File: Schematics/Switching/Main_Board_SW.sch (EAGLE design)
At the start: 88 parts, among them IC1 LM317MBSTT3, IC2 LM317MBSTT3, Q1 32.768kHz, X1 MINI-USB-SHIELD-UX60-MB-5ST, X2 RJ45

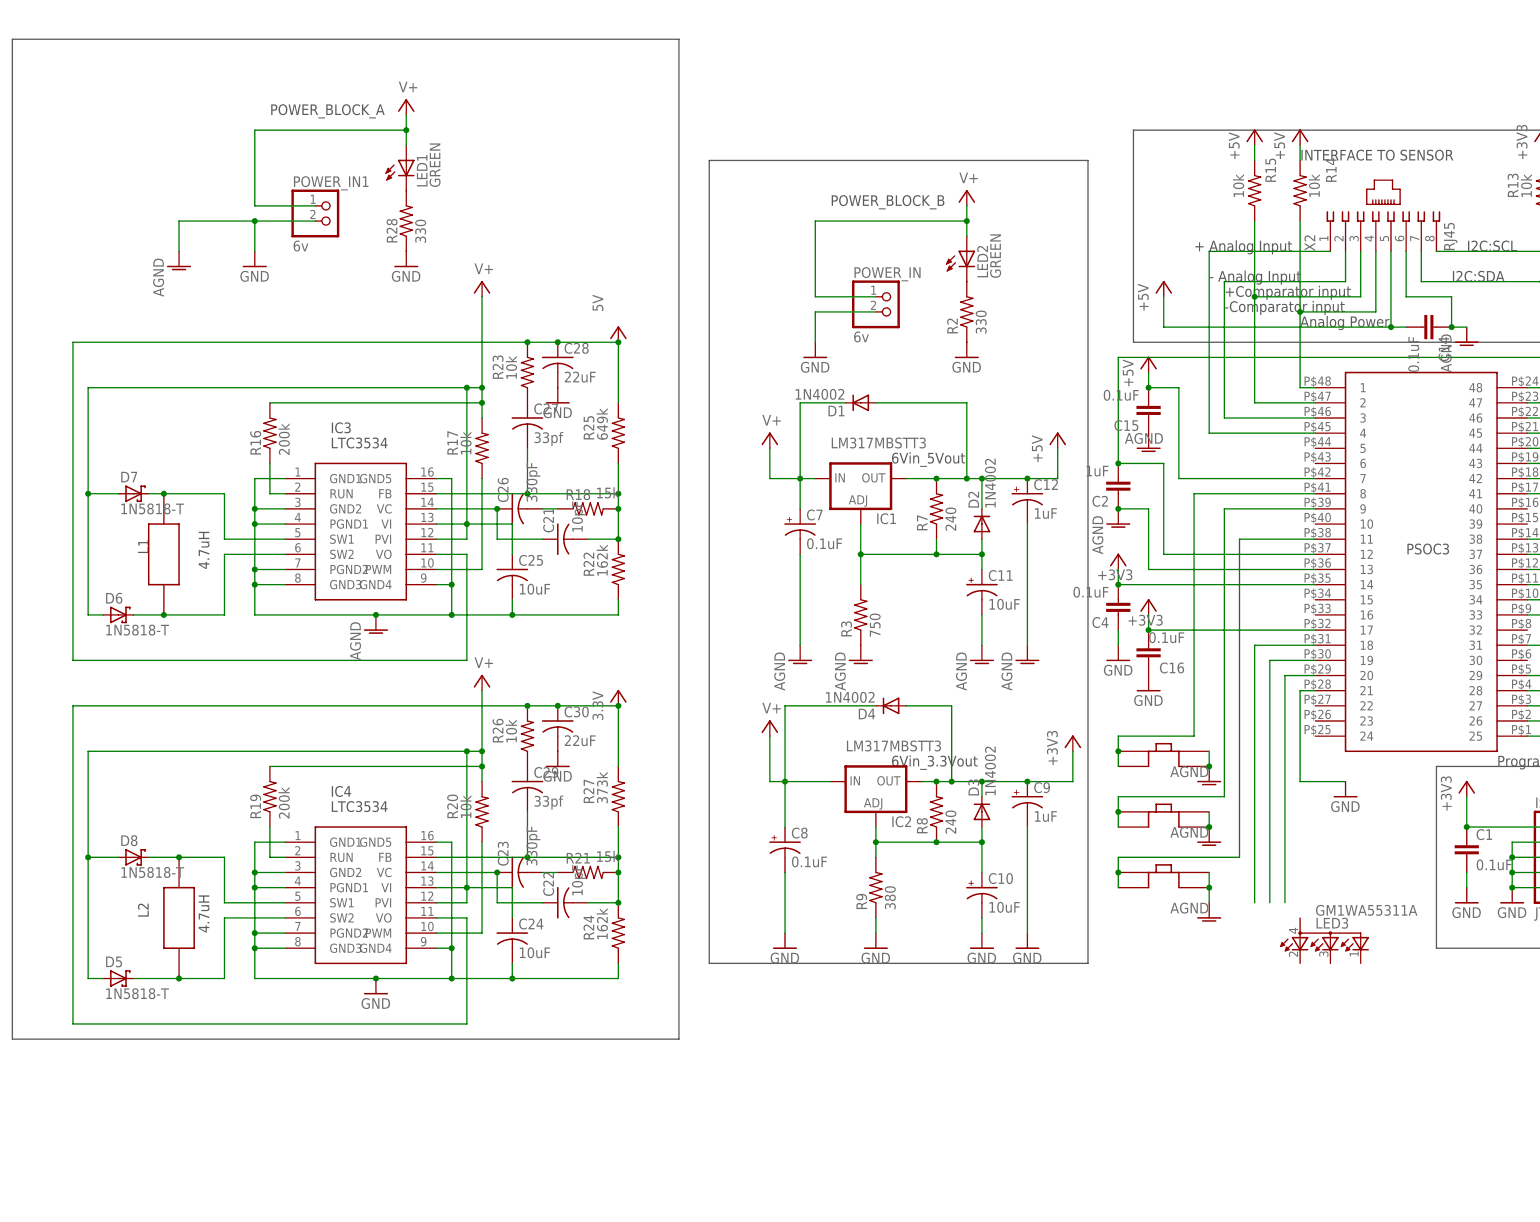
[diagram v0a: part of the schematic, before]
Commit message: Updates for pin assignments
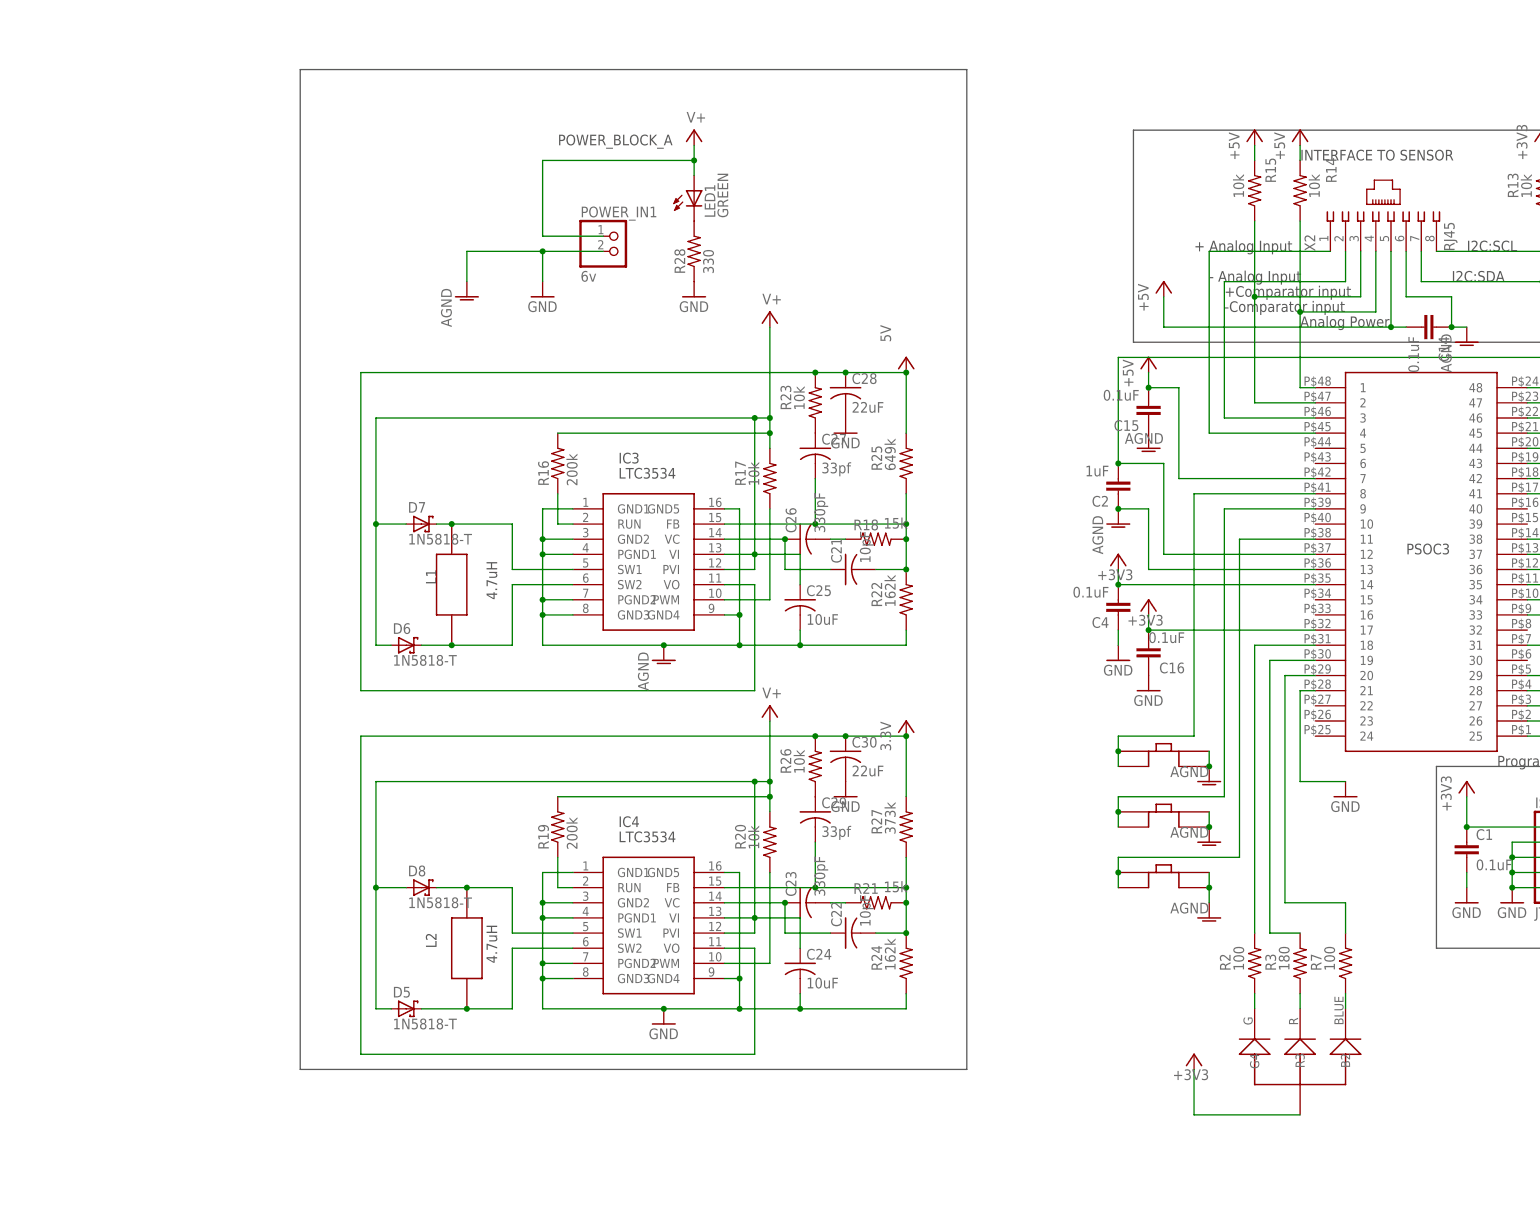
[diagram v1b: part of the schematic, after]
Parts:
- removed C10, C11: 10uF, rcl:CPOL-USE2-5
- removed C12, C9: 1uF, rcl:CPOL-USE2-5
- removed C7, C8: 0.1uF, rcl:CPOL-USE2-5
- removed D1, D2, D3, D4: 1N4002, diode:DIODE-DO41-7.6
- removed IC1, IC2: LM317MBSTT3, v-reg:LM317MBSTT3
- removed LED2: GREEN, led:LED5MM
- removed LED3: GM1WA55311A, led:GM1WA55311A
- removed POWER_IN: 6v, pinhead:PINHD-1X2
- removed R8: 240, rcl:R-US_M1206
- removed R9: 380, rcl:R-US_M1206
- added U$7: RGB_LED, RGB_LED:RGB_LED
- R2: value 330 -> 100; device rcl:R-US_R0603 -> rcl:R-US_R0805
- R3: value 750 -> 180; device rcl:R-US_M1206 -> rcl:R-US_R0805
- R7: value 240 -> 100; device rcl:R-US_M1206 -> rcl:R-US_R0805
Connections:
- net +3V3: now also U$7.VCC1; no longer C9.+, D3.C, D4.A, IC2.OUT, R8.2
- net +5V: no longer C12.+, D1.A, D2.C, IC1.OUT, R7.2
- net GND: no longer C10.-, C11.-, C12.-, C7.-, C8.-, C9.-, POWER_IN.2, R2.1, R3.1, R9.1
- net N$10: now also R2.1, U$7.G4; no longer C11.+, D2.A, IC1.ADJ, R3.2, R7.1
- net N$12: now also R3.1, U$7.R3; no longer LED2.C, R2.2
- net N$15: now also R7.1, U$7.B2; no longer C10.+, D3.A, IC2.ADJ, R8.1, R9.2
- net N$43: now also R2.2
- net N$46: now also R3.2
- net N$47: now also R7.2
- net V+: no longer C7.+, C8.+, D1.C, D4.C, IC1.IN, IC2.IN, LED2.A, POWER_IN.1
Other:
- note removed: "6Vin_3.3Vout"
- note removed: "6Vin_5Vout"
- note removed: "POWER_BLOCK_B"
- moved on the sheet: C21, C22, C23, C24, C25, C26, C27, C28, C29, C30, D5, D6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

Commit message: Pin updates and initial board push
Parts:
- removed LED1: GREEN, led:LED5MM
- removed R28: 330, rcl:R-US_R0603
- renumbered U$2 to SWA, U$3 to SWD
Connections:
- removed net N$40: LED1.C, R28.2
- new net PE: C13.1, R10.1, X1.GND1, X1.GND2, X1.GND3, X1.GND4
- net +3V3: now also C16.2, C30.1, R26.2, R27.2, SWD.VO, U$1.17
- net +5V: now also C28.1, R23.2, R25.2, SWA.VO; no longer C16.2, U$1.17
- net AGND: now also C14.1, C15.1, C2.1, C3.1, C6.1, U$1.13, U$1.47, X2.6; no longer C13.1, R10.1, X1.GND1, X1.GND2, X1.GND3, X1.GND4
- net GND: now also X1.4; no longer C14.1, C15.1, C2.1, C3.1, C6.1, R28.1, U$1.13, U$1.47, X2.6
- net V+: no longer C28.1, C30.1, LED1.A, R23.2, R25.2, R26.2, R27.2, SWA.VO, SWD.VO

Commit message: Button Updates
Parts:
- removed U$4: SPST, Switches_SPST:SPST
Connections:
- removed net N$45: U$1.8, U$4.A1, U$4.A2
- net +3V3: now also U$5.B1, U$5.B2, U$6.B1, U$6.B2
- net AGND: no longer U$4.B1, U$4.B2, U$5.B1, U$5.B2, U$6.B1, U$6.B2
- net N$41: now also U$1.15; no longer U$1.9
- net N$44: now also U$1.16; no longer U$1.11
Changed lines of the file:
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@@
 <part name="SUPPLY8" library="supply2" deviceset="V+" device=""/>
 <part name="FRAME1" library="frames" deviceset="FRAME_B_L" device="" value="3"/>
-<part name="U$4" library="Switches_SPST" deviceset="SPST" device=""/>
 <part name="U$5" library="Switches_SPST" deviceset="SPST" device=""/>
 <part name="U$6" library="Switches_SPST" deviceset="SPST" device=""/>
-<part name="GND35" library="supply1" deviceset="AGND" device=""/>
-<part name="GND36" library="supply1" deviceset="AGND" device=""/>
-<part name="GND37" library="supply1" deviceset="AGND" device=""/>
 <part name="U$7" library="RGB_LED" deviceset="RGB_LED" device=""/>
 <part name="R2" library="rcl" deviceset="R-US_" device="R0805" value="100"/>
@@
 <part name="PE2" library="supply1" deviceset="PE" device=""/>
 <part name="GND4" library="supply1" deviceset="GND" device=""/>
+<part name="+3V12" library="supply1" deviceset="+3V3" device=""/>
+<part name="+3V13" library="supply1" deviceset="+3V3" device=""/>
 </parts>
 <sheets>
@@
 <attribute name="DRAWING_NAME" x="137.16" y="-72.39" size="2.54" layer="94" font="vector"/>
 </instance>
-<instance part="U$4" gate="G$1" x="25.4" y="10.16"/>
 <instance part="U$5" gate="G$1" x="25.4" y="0"/>
 <instance part="U$6" gate="G$1" x="25.4" y="-10.16"/>
-<instance part="GND35" gate="VR1" x="35.56" y="7.62" smashed="yes">
-<attribute name="VALUE" x="35.56" y="10.16" size="1.778" layer="96" rot="R180"/>
-</instance>
-<instance part="GND36" gate="VR1" x="35.56" y="-2.54" smashed="yes">
-<attribute name="VALUE" x="35.56" y="0" size="1.778" layer="96" rot="R180"/>
-</instance>
-<instance part="GND37" gate="VR1" x="35.56" y="-15.24" smashed="yes">
-<attribute name="VALUE" x="35.56" y="-12.7" size="1.778" layer="96" rot="R180"/>
-</instance>
 <instance part="U$7" gate="G$1" x="50.8" y="-43.18" rot="R180"/>
 <instance part="R2" gate="G$1" x="43.18" y="-22.86" smashed="yes" rot="R90">
@@
 </instance>
 <instance part="GND4" gate="1" x="-58.42" y="27.94"/>
+<instance part="+3V12" gate="G$1" x="12.7" y="10.16" smashed="yes">
+<attribute name="VALUE" x="10.16" y="5.08" size="1.778" layer="96" rot="R90"/>
+</instance>
+<instance part="+3V13" gate="G$1" x="10.16" y="-7.62" smashed="yes">
+<attribute name="VALUE" x="12.7" y="-10.16" size="1.778" layer="96" rot="R90"/>
+</instance>
 </instances>
 <busses>
@@
 <pinref part="+3V9" gate="G$1" pin="+3V3"/>
 </segment>
+<segment>
+<wire x1="35.56" y1="-2.54" x2="12.7" y2="-2.54" width="0.1524" layer="91"/>
+<wire x1="12.7" y1="-2.54" x2="12.7" y2="7.62" width="0.1524" layer="91"/>
+<pinref part="U$5" gate="G$1" pin="B1"/>
+<pinref part="U$5" gate="G$1" pin="B2"/>
+<wire x1="35.56" y1="2.54" x2="35.56" y2="0" width="0.1524" layer="91"/>
+<wire x1="35.56" y1="-2.54" x2="35.56" y2="0" width="0.1524" layer="91"/>
+<junction x="35.56" y="0"/>
+<pinref part="+3V12" gate="G$1" pin="+3V3"/>
+</segment>
+<segment>
+<pinref part="U$6" gate="G$1" pin="B1"/>
+<pinref part="U$6" gate="G$1" pin="B2"/>
+<wire x1="35.56" y1="-7.62" x2="35.56" y2="-10.16" width="0.1524" layer="91"/>
+<wire x1="35.56" y1="-10.16" x2="35.56" y2="-12.7" width="0.1524" layer="91"/>
+<junction x="35.56" y="-10.16"/>
+<wire x1="35.56" y1="-12.7" x2="10.16" y2="-12.7" width="0.1524" layer="91"/>
+<wire x1="10.16" y1="-12.7" x2="10.16" y2="-10.16" width="0.1524" layer="91"/>
+<pinref part="+3V13" gate="G$1" pin="+3V3"/>
+</segment>
 </net>
 <net name="V+" class="0">
@@
 <net name="AGND" class="0">
 <segment>
-<pinref part="U$4" gate="G$1" pin="B1"/>
-<pinref part="U$4" gate="G$1" pin="B2"/>
-<wire x1="35.56" y1="12.7" x2="35.56" y2="10.16" width="0.1524" layer="91"/>
-<junction x="35.56" y="10.16"/>
-<pinref part="GND35" gate="VR1" pin="AGND"/>
-</segment>
-<segment>
-<pinref part="U$5" gate="G$1" pin="B1"/>
-<pinref part="U$5" gate="G$1" pin="B2"/>
-<wire x1="35.56" y1="2.54" x2="35.56" y2="0" width="0.1524" layer="91"/>
-<junction x="35.56" y="0"/>
-<pinref part="GND36" gate="VR1" pin="AGND"/>
-</segment>
-<segment>
-<pinref part="GND37" gate="VR1" pin="AGND"/>
-<wire x1="35.56" y1="-10.16" x2="35.56" y2="-12.7" width="0.1524" layer="91"/>
-<pinref part="U$6" gate="G$1" pin="B1"/>
-<pinref part="U$6" gate="G$1" pin="B2"/>
-<wire x1="35.56" y1="-7.62" x2="35.56" y2="-10.16" width="0.1524" layer="91"/>
-<junction x="35.56" y="-10.16"/>
-</segment>
-<segment>
 <pinref part="C15" gate="G$1" pin="1"/>
 <pinref part="AGND3" gate="VR1" pin="AGND"/>
@@
 </segment>
 </net>
-<net name="N$45" class="0">
-<segment>
-<pinref part="U$4" gate="G$1" pin="A2"/>
-<pinref part="U$4" gate="G$1" pin="A1"/>
-<wire x1="20.32" y1="10.16" x2="20.32" y2="12.7" width="0.1524" layer="91"/>
-<wire x1="20.32" y1="12.7" x2="20.32" y2="15.24" width="0.1524" layer="91"/>
-<junction x="20.32" y="12.7"/>
-<wire x1="20.32" y1="15.24" x2="33.02" y2="15.24" width="0.1524" layer="91"/>
-<wire x1="33.02" y1="15.24" x2="33.02" y2="55.88" width="0.1524" layer="91"/>
-<pinref part="U$1" gate="G$1" pin="8"/>
-<wire x1="53.34" y1="55.88" x2="33.02" y2="55.88" width="0.1524" layer="91"/>
-</segment>
-</net>
 <net name="N$41" class="0">
 <segment>
@@
 <wire x1="20.32" y1="2.54" x2="20.32" y2="5.08" width="0.1524" layer="91"/>
 <wire x1="20.32" y1="5.08" x2="38.1" y2="5.08" width="0.1524" layer="91"/>
-<wire x1="38.1" y1="5.08" x2="38.1" y2="53.34" width="0.1524" layer="91"/>
-<pinref part="U$1" gate="G$1" pin="9"/>
-<wire x1="38.1" y1="53.34" x2="53.34" y2="53.34" width="0.1524" layer="91"/>
 <pinref part="U$5" gate="G$1" pin="A2"/>
 <wire x1="20.32" y1="0" x2="20.32" y2="2.54" width="0.1524" layer="91"/>
 <junction x="20.32" y="2.54"/>
+<wire x1="38.1" y1="5.08" x2="38.1" y2="38.1" width="0.1524" layer="91"/>
+<pinref part="U$1" gate="G$1" pin="15"/>
+<wire x1="38.1" y1="38.1" x2="53.34" y2="38.1" width="0.1524" layer="91"/>
 </segment>
 </net>
@@
 <junction x="20.32" y="-7.62"/>
 <wire x1="20.32" y1="-5.08" x2="40.64" y2="-5.08" width="0.1524" layer="91"/>
-<wire x1="40.64" y1="-5.08" x2="40.64" y2="48.26" width="0.1524" layer="91"/>
-<pinref part="U$1" gate="G$1" pin="11"/>
-<wire x1="40.64" y1="48.26" x2="53.34" y2="48.26" width="0.1524" layer="91"/>
-</segment>
-</net>
+<wire x1="40.64" y1="-5.08" x2="40.64" y2="35.56" width="0.1524" layer="91"/>
+<pinref part="U$1" gate="G$1" pin="16"/>
+<wire x1="40.64" y1="35.56" x2="53.34" y2="35.56" width="0.1524" layer="91"/>
+</segment>
+</net>

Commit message: Stuff
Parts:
- added C10, C31: 47uF, rcl:C-USC1210
- added C11, C32: 1uF, rcl:C-USC0603
- added C12, C9: 1000pF, rcl:C-USC0402
- added C7, C8: 0.047uF, rcl:C-USC0402
- added R8, R9: 2, rcl:R-US_R0402
- D5, D6, D7, D8: value 1N5818-T -> (none); device diode:1N5818-T -> diode:DIODE-SOD323-R
- ISP: device pinhead:PINHD-2X5/90 -> con-samtec:FTSH-105-01-L-DV-K
- R16: value 200k -> 499K
- R19: value 200k -> 499k
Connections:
- removed net AGND: C14.1, C15.1, C2.1, C3.1, C6.1, U$1.13, U$1.47, X2.6
- removed net N$21: R12.1, U$1.42, X2.8
- new net N$130: C9.2, R8.2
- new net N$131: C12.2, R9.2
- new net N$61: R13.1, U$1.43, X2.2
- net +3V3: now also C32.1, D5.C
- net +5V: now also C11.1, D6.C, X2.4; no longer X2.5
- net ANALOGINPUT: now also X2.8; no longer X2.2
- net GND: now also C10.2, C11.2, C14.1, C15.1, C2.1, C3.1, C31.2, C32.2, C6.1, C7.2, C8.2, D7.A, D8.A, R8.1, R9.1, U$1.13, U$1.47, X2.3
- net N$18: now also X2.5; no longer X2.3
- net N$19: now also X2.6; no longer X2.4
- net N$20: now also R12.1, U$1.42, X2.1; no longer R13.1, U$1.43, X2.7
- net N$25: now also C7.1
- net N$26: now also C9.1
- net N$28: now also D6.A; no longer D6.C
- net N$32: now also C8.1
- net N$34: now also C12.1
- net N$35: now also D5.A; no longer D5.C
- net N$42: now also X2.7; no longer X2.1
- net V+: now also C10.1, C31.1; no longer D5.A, D6.A, D7.A, D8.A
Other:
- note added: "3.3uH"
- note removed: "4.7uH"
- moved on the sheet: R12, R13, R14, R15, R22, R25, X2

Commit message: Layout Update
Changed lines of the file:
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@@
 <wire x1="-116.84" y1="-40.64" x2="-116.84" y2="127" width="0.1524" layer="97"/>
 <text x="114.3" y="127" size="6.4516" layer="97">Erebus Labs </text>
-<text x="104.14" y="129.54" size="6.4516" layer="97">Main Sensor Board</text>
+<text x="106.68" y="134.62" size="6.4516" layer="97">Main Sensor Board</text>
 <text x="132.08" y="104.14" size="6.4516" layer="97">Rev 2</text>
 <text x="-63.5" y="60.96" size="1.778" layer="97">IC3</text>

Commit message: Added Drill Holes. Moved Traces. Moved Silkscreen References
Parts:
- added H1, H2, H3, H4: MOUNT-HOLE2.8, holes:MOUNT-HOLE2.8
- renumbered SWA to REGULATOR_5, SWD to REGULATOR_3.3, U$7 to RGB_LED

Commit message: Layout for final inspection
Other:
- note added: "B1"
- note added: "B2"
- note added: "D10"
- note added: "RGB"
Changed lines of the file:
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@@
 <?xml version="1.0" encoding="utf-8"?>
 <!DOCTYPE eagle SYSTEM "eagle.dtd">
-<eagle version="6.3">
+<eagle version="6.4">
 <drawing>
 <settings>
@@
 <text x="213.36" y="-83.82" size="2.54" layer="94">2</text>
 <text x="134.62" y="-91.44" size="2.54" layer="94">4/28/2014</text>
+<text x="53.34" y="-43.18" size="1.778" layer="95">D10</text>
+<text x="53.34" y="-45.72" size="1.778" layer="95">RGB</text>
+<text x="27.94" y="-10.16" size="1.778" layer="95">B1</text>
+<text x="27.94" y="0" size="1.778" layer="95">B2</text>
 </plain>
 <instances>
